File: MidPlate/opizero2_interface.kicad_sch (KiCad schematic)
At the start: 1 part

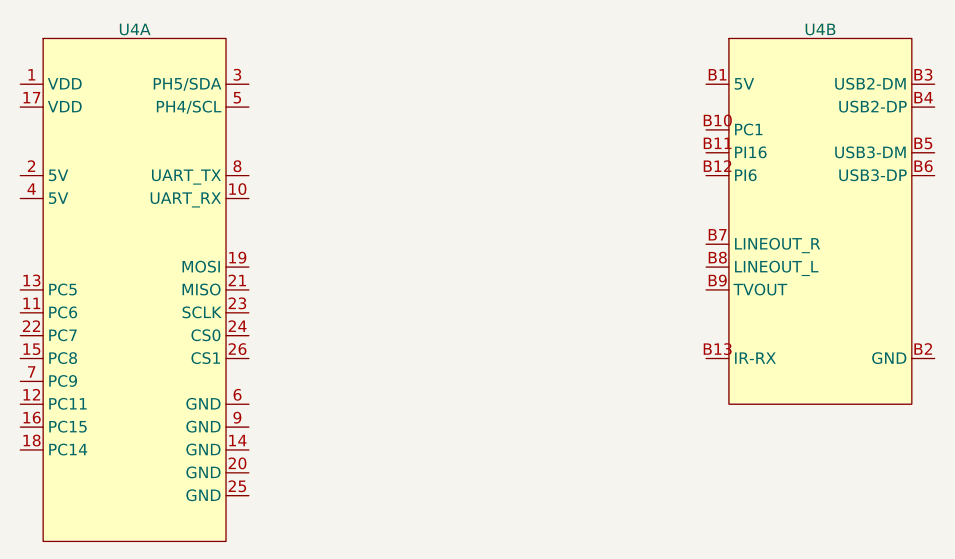
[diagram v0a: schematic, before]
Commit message: update to power board and midplate schematics
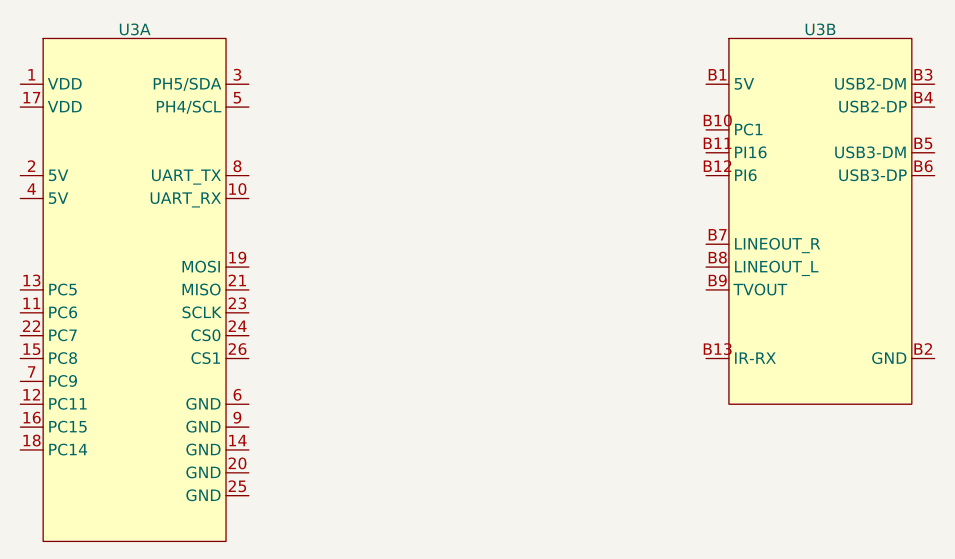
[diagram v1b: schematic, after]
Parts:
- renumbered U4 to U3
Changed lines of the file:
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@@
   (symbol (lib_id "thebots_midplate:OrangePiZero2") (at 177.8 71.12 0) (unit 2)
     (in_bom yes) (on_board yes) (dnp no) (fields_autoplaced)
-    (property "Reference" "U4" (at 177.8 49.8381 0)
+    (property "Reference" "U3" (at 177.8 49.8381 0)
       (effects (font (size 1.27 1.27)))
     )
@@
       (project "midplate"
         (path "/69058343-dac8-421b-a3f6-e069eb1ba8ae/2f59e60a-c040-428f-85de-f426839730b7"
-          (reference "U4") (unit 2)
+          (reference "U3") (unit 2)
         )
       )
@@
   (symbol (lib_id "thebots_midplate:OrangePiZero2") (at 101.6 78.74 0) (unit 1)
     (in_bom yes) (on_board yes) (dnp no) (fields_autoplaced)
-    (property "Reference" "U4" (at 101.6 49.8381 0)
+    (property "Reference" "U3" (at 101.6 49.8381 0)
       (effects (font (size 1.27 1.27)))
     )
@@
       (project "midplate"
         (path "/69058343-dac8-421b-a3f6-e069eb1ba8ae/2f59e60a-c040-428f-85de-f426839730b7"
-          (reference "U4") (unit 1)
+          (reference "U3") (unit 1)
         )
       )

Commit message: powerboard HV powerpillars + midplate
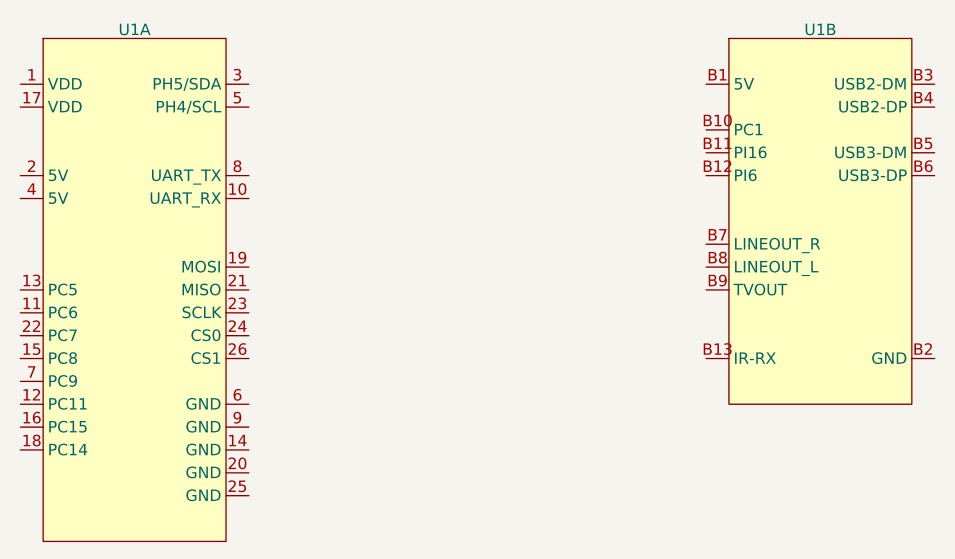
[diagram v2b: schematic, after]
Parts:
- renumbered U3 to U1
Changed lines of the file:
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@@
   (symbol (lib_id "thebots_midplate:OrangePiZero2") (at 177.8 71.12 0) (unit 2)
     (in_bom yes) (on_board yes) (dnp no) (fields_autoplaced)
-    (property "Reference" "U3" (at 177.8 49.8381 0)
+    (property "Reference" "U1" (at 177.8 49.8381 0)
       (effects (font (size 1.27 1.27)))
     )
@@
       (project "midplate"
         (path "/69058343-dac8-421b-a3f6-e069eb1ba8ae/2f59e60a-c040-428f-85de-f426839730b7"
-          (reference "U3") (unit 2)
+          (reference "U1") (unit 2)
         )
       )
@@
   (symbol (lib_id "thebots_midplate:OrangePiZero2") (at 101.6 78.74 0) (unit 1)
     (in_bom yes) (on_board yes) (dnp no) (fields_autoplaced)
-    (property "Reference" "U3" (at 101.6 49.8381 0)
+    (property "Reference" "U1" (at 101.6 49.8381 0)
       (effects (font (size 1.27 1.27)))
     )
@@
       (project "midplate"
         (path "/69058343-dac8-421b-a3f6-e069eb1ba8ae/2f59e60a-c040-428f-85de-f426839730b7"
-          (reference "U3") (unit 1)
+          (reference "U1") (unit 1)
         )
       )
